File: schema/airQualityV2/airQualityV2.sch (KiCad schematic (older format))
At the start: 17 parts, among them J1 mhz19, J2 ccs811, J3 Conn_01x04_Female, U1 ESP32_DevKit_V1_DOIT

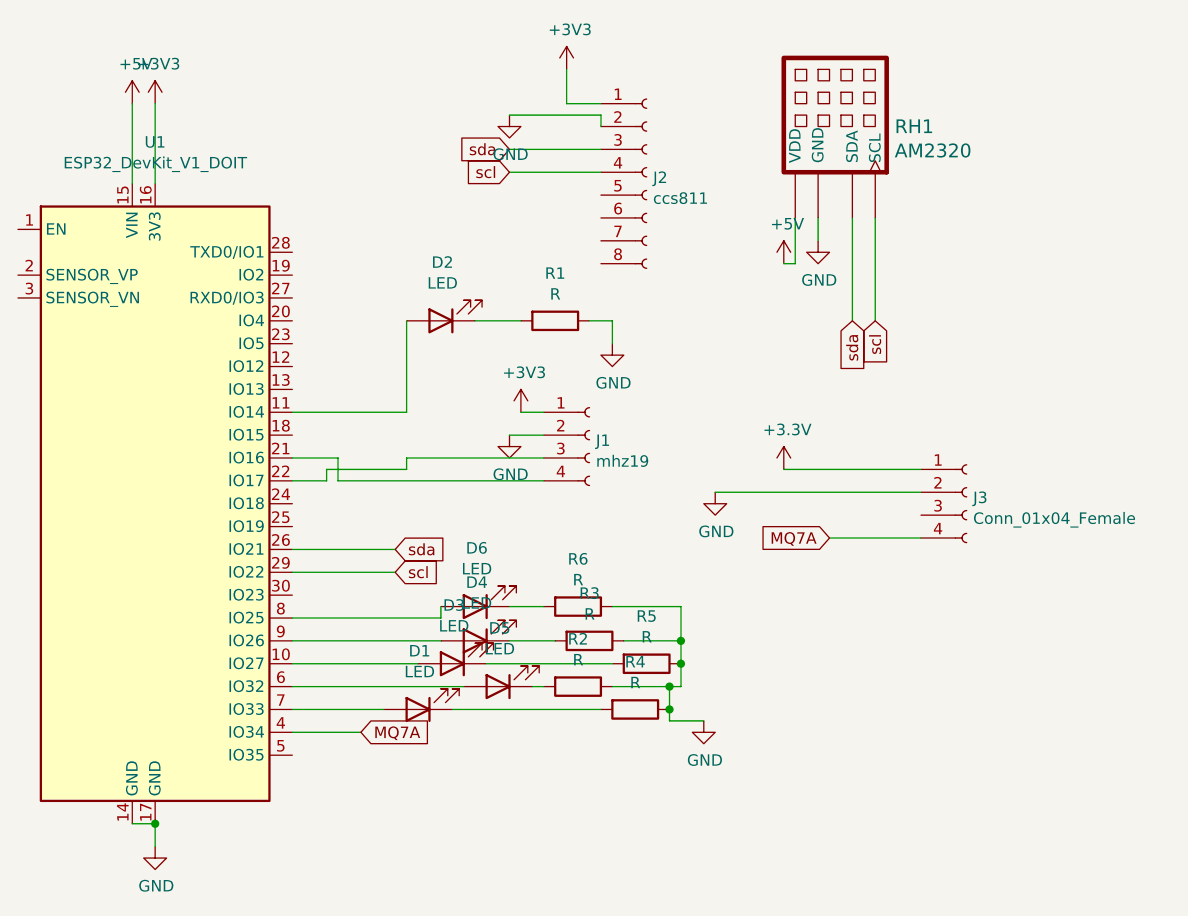
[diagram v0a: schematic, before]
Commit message: update schematic
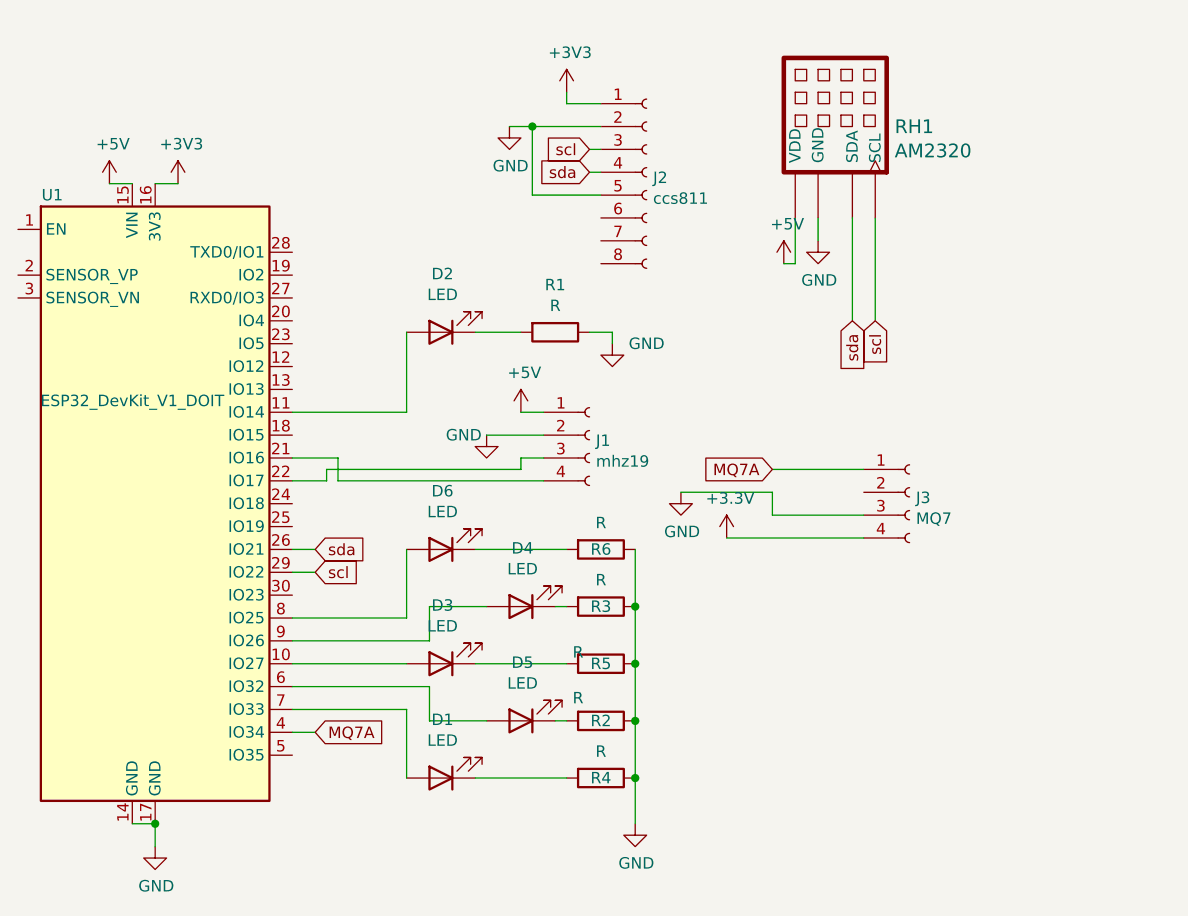
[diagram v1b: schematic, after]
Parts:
- J3: value Conn_01x04_Female -> MQ7
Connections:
- net +3V3: now also J3.4 (Pin_4); no longer J1.1 (Pin_1), J3.1 (Pin_1)
- net +5V: now also J1.1 (Pin_1)
- net GND: now also J2.5 (Pin_5), J3.3 (Pin_3); no longer J3.2 (Pin_2)
- net MQ7A: now also J3.1 (Pin_1); no longer J3.4 (Pin_4)
- net scl: now also J2.3 (Pin_3); no longer J2.4 (Pin_4)
- net sda: now also J2.4 (Pin_4); no longer J2.3 (Pin_3)
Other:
- moved on the sheet: D1, D2, D3, D4, D5, D6, J3, R1, R2, R3, R4, R5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
